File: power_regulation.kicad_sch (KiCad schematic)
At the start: 101 parts, among them IC2 PJA3402_R1_00001, IC3 MIE1W0505BGLVH-3R-P, J12 Conn_01x02_Pin, J6 V_bat_secondary, J7 Conn_01x02_Pin, J8 Conn_01x02_Pin, J9 Conn_01x02_Pin, U10 TPS7A2045PDBVR, U11 TPS7A2018PDBVRG4, U12 TPS7A2033PDBVR, U13 TPS7A2033PDBVR, U14 TLV75733PDYDR, U15 TPS7A2033PDBVR, U5 TPS7A2042PDBVRG4, U6 MCP1501-30xCH, U7 TPS62933, U8 TPS62933, U9 OPA387DBVR

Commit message: Commit before 5V rebase.
[KiCad Version: 10.0.4]
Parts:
- added C? (x4): 1u, Capacitor_SMD:C_0603_1608Metric_Pad1.08x0.95mm_HandSolder, symbol Device:C
- added R32: 100k, Resistor_SMD:R_0603_1608Metric_Pad0.98x0.95mm_HandSolder, symbol Device:R
- added U?: TPS7A2033PDBVR, Package_TO_SOT_SMD:SOT-23-5, symbol Regulator_Linear:TPS7A0508PDBV
- added Vref?: TestPoint, TestPoint:TestPoint_Pad_D1.0mm, symbol Connector:TestPoint
- C74: renamed from C64; now not fitted; now left out of the parts list
- renumbered C34 to C41, C35 to C42, C36 to C43, C37 to C44, C38 to C45, C39 to C46, C40 to C47, C41 to C48, C42 to C49, C43 to C50, C44 to C51, C45 to C52, C46 to C53, C47 to C54, C48 to C55, C49 to C56, C50 to C57, C51 to C58, C52 to C59, C53 to C60, C54 to C61, C55 to C62, C105 to C63, C56 to C64, C57 to C65, C58 to C66, C59 to C67, C60 to C68, C61 to C69, C62 to C70, C63 to C71, C67 to C72, C70 to C73, C65 to C75, C66 to C76, C68 to C77, C75 to C78, C69 to C79, C71 to C80, C72 to C81, C73 to C82, C80 to C83, C100 to C84, C74 to C85, C101 to C86, C76 to C87, C98 to C88, C77 to C89, C78 to C90, C79 to C91, C99 to C92, C81 to C93, C102 to C94, C82 to C95, C103 to C96, C104 to C97, D3 to D5, D4 to D6, J7 to J10, J8 to J11, J9 to J12, J12 to J13, J6 to J9, R21 to R20, R22 to R21, R23 to R22, R24 to R23, R25 to R24, R26 to R25, R27 to R26, R28 to R27, R29 to R28, R30 to R29, R31 to R30, R32 to R31, U9 to U10, U10 to U11, U11 to U13, U13 to U14, U14 to U15, U15 to U16, U5 to U6, U6 to U7, U7 to U8, U8 to U9
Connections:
- net +3V3_Ana: now also C?.2, C?.2, U?.5 (OUT), Vref?.1
- net +4V2_bus: no longer C44.2, C45.2, C46.2, U6.5 (OUT), U7.4 (~{SHDN}), U7.6 (VDD)
- net +5V_buck_out: no longer C59.2, C62.2, C70.2, C71.2, C82.2, IC3.10 (VIN_2), IC3.14 (VIN_3), IC3.8 (EN), IC3.9 (VIN_1), Lw1.2, R25.1, U11.1 (IN), U11.3 (EN), U15.1 (IN), U15.3 (EN)
- net GND: now also C?.1, C?.1, C?.1, C?.1, U?.2 (GND)
- new net: C44.2, C45.2, C46.2, U6.5 (OUT), U7.4 (~{SHDN}), U7.6 (VDD)
- new net: IC3.8 (EN), R32.2
- new net +5V_Ana_Bus: C?.2, C?.2, U?.1 (IN), U?.3 (EN)
- new net +Buck_Out: C59.2, C62.2, C70.2, C71.2, C82.2, IC3.10 (VIN_2), IC3.14 (VIN_3), IC3.9 (VIN_1), Lw1.2, R25.1, R32.1, U11.1 (IN), U11.3 (EN), U15.1 (IN), U15.3 (EN)
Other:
- note added: "3,3V ANALOG SUPPLY LDO Supplies Load Cell, Load Cell ADC and the 1V8 LDO"
- note added: "Isolating DCDC Converter for Voltage Measurement"
- note added: "SAR ADC Vref Driver"
- note added: "TODO: Change symbol to MCP1502!!!"
- note added: "TODO: Check Min / Max stable capacitances for the LDOS"
- note removed: "TARKASTA MINIMI STABLE KAPASITANSSIT TÄLLE !!"
- note removed: "TÄHÄN MCP1502 !!!"
- moved on the sheet: C70, C71, C75, C77, C79, C81, C82, C85, C89, C90, C93, C95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

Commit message: Implemented SAR ADC Buffering on top layer with one OPA387
[KiCad Version: 10.0.4]
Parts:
- removed C41, C42, C44, C45, C66, C? (x4): 1u, Capacitor_SMD:C_0603_1608Metric_Pad1.08x0.95mm_HandSolder, symbol Device:C
- removed C83, C85, C90, C93: 2.2u, Capacitor_SMD:C_0603_1608Metric_Pad1.08x0.95mm_HandSolder, symbol Device:C
- removed C94: 22u, Capacitor_SMD:C_1206_3216Metric_Pad1.33x1.80mm_HandSolder, symbol Device:C
- removed IC2: PJA3402_R1_00001, SOT95P240X110-3N, symbol SamacSys_Parts:PJA3402_R1_00001
- removed J10: Conn_01x02_Pin, Connector_PinHeader_2.54mm:PinHeader_1x02_P2.54mm_Vertical, symbol Connector:Conn_01x02_Pin
- removed R30: 220, Resistor_SMD:R_0603_1608Metric_Pad0.98x0.95mm_HandSolder, symbol Device:R
- removed U6: TPS7A2042PDBVRG4, Package_TO_SOT_SMD:SOT-23-5, symbol Regulator_Linear:TPS7A0508PDBV
- removed U?: TPS7A2033PDBVR, Package_TO_SOT_SMD:SOT-23-5, symbol Regulator_Linear:TPS7A0508PDBV
- removed Vref?: TestPoint, TestPoint:TestPoint_Pad_D1.0mm, symbol Connector:TestPoint
- added C101, C102, C104, C49, C61, C64, C65, C70, C75, C79, C80, C81, C82, C88: 1u, Capacitor_SMD:C_0603_1608Metric_Pad1.08x0.95mm_HandSolder, symbol Device:C
- added C62: 4.7nF, Capacitor_SMD:C_0603_1608Metric_Pad1.08x0.95mm_HandSolder, symbol Device:C
- added C72: 10u, Capacitor_SMD:C_0603_1608Metric_Pad1.08x0.95mm_HandSolder, symbol Device:C
- added DIO2: TestPoint, TestPoint:TestPoint_Pad_D1.0mm, symbol Connector:TestPoint
- added IC?: OPA2387DR, SOIC127P600X175-8N, symbol SamacSys_Parts:OPA2387DR
- added R32: 0R, Resistor_SMD:R_0603_1608Metric_Pad0.98x0.95mm_HandSolder, symbol Device:R
- added U12, U15: TPS7A2050PDBVR, Package_TO_SOT_SMD:SOT-23-5, symbol Regulator_Linear:TPS7A0508PDBV
- added U14: TPS7A2033PDBVR, Package_TO_SOT_SMD:SOT-23-5, symbol Regulator_Linear:TPS7A0508PDBV
- C60: now fitted
- C68: renamed from C67; value 10u -> 1u
- C78, C87, C89, C91: value 2.2u -> 1u
- C84, C86: value 22u -> 1u; footprint Capacitor_SMD:C_1206_3216Metric_Pad1.33x1.80mm_HandSolder -> Capacitor_SMD:C_0603_1608Metric_Pad1.08x0.95mm_HandSolder; now fitted; now in the parts list
- R25: value 52.3k -> 63k
- R29: renamed from R22; value 7.87k -> 8.2k
- R30: renamed from R24; value 11k -> 10k
- R33: renamed from R29; value 5R -> 1R
- R35: renamed from R33; now not fitted; now left out of the parts list
- R36: renamed from R34; now not fitted; now left out of the parts list
- R37: renamed from R35; now not fitted; now left out of the parts list
- U10: renamed from U11; value TPS7A2045PDBVR -> TPS7A2055PDBVR; Manufacturing_Number TPS7A2045PDBVR -> TPS7A2055PDBVR; Mouser_nro (none) -> 595-TPS7A2055PDBVR
- U17: renamed from U12; value TPS7A2033PDBVR -> TPS7A2050PDBVR; Manufacturing_Number (none) -> TPS7A2050PDBVR
- U18: renamed from U16; value TPS7A2033PDBVR -> TPS7A2045PDBVR; Manufacturing_Number (none) -> TPS7A2045PDBVR
- U8: renamed from U7; value MCP1501-30xCH -> MCP1502T-50E/CHY
- renumbered C96 to C100, C97 to C103, C95 to C105, C50 to C43, C47 to C44, C52 to C45, C48 to C46, C49 to C47, C54 to C48, C46 to C50, C43 to C51, C55 to C52, C57 to C53, C51 to C54, C61 to C55, C53 to C56, C59 to C57, C62 to C58, C56 to C59, C58 to C63, C82 to C66, C63 to C67, C64 to C69, C65 to C71, C68 to C73, C69 to C74, C80 to C77, C70 to C83, C71 to C85, C74 to C90, C88 to C92, C92 to C93, C75 to C94, C72 to C95, C79 to C96, C77 to C97, C73 to C98, C81 to C99, J11 to J10, J12 to J11, J13 to J12, R21 to R22, R20 to R24, R32 to R34, U15 to U11, U14 to U13, U13 to U16, U8 to U6, U9 to U7, U10 to U9
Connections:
- net +4V2_bus is gone; now on net +5V5_bus: C63.2, U9.5 (V+)
- net +5V_buck_out is gone; now on net GND: C60.1
- net +1V8_MCP_AVIN: now also C101.2, C104.2; no longer C89.2
- net +3V3_DIO: now also C84.2, C86.2; no longer C87.2, C91.2
- net +3V3_ESP: now also C72.2
- net GND: now also C101.1, C102.1, C104.1, C49.1, C61.2, C64.1, C65.2, C70.2, C72.1, C75.1, C79.1, C80.1, C81.1, C82.1, C88.1, U12.2 (GND), U14.2 (GND), U15.2 (GND); no longer C60.2, R31.1
- net +5V5_bus: now reaches C50.2, U8.4 (~{SHDN}), U8.6 (VDD)
- net +5V5_bus: now also C68.1, C73.2, C74.2, C76.2, C77.2, C95.2, C98.2, U10.5 (OUT), U13.1 (IN), U13.3 (EN), U17.1 (IN), U17.3 (EN), C49.2, C70.1, C80.2, C82.2, U15.1 (IN), U15.3 (EN)
- net +12V_Fan_Supply: now reaches D6.2 (A), J10.2 (Pin_2)
- net +5V_Vref: now reaches R31.2
- net +5V_Vref: now also C67.2, C69.2, C71.2, R33.2, Vref1.1
- net at C59.2, R33.1, U9.1: now also R32.2
- net at R30.2, U9.3 (+): now also C60.2
- net +3V3_Ana renamed +5V_Ana
- net +5V_Ana: now also C89.2, C91.2, Vref2.1, C79.2, U14.1 (IN), U14.3 (EN), U15.5 (OUT); no longer C84.2, C86.2, U17.5 (OUT), Vref3.1
- net +3V3_ISO renamed +4V5_ISO
- removed net +3V_Vref: C67.2, C69.2, C71.2, R33.2, U9.4 (-), Vref1.1
- removed net +4V5_bus: C68.1, C73.2, C74.2, C76.2, C77.2, C95.2, C98.2, U10.5 (OUT), U13.1 (IN), U13.3 (EN), U17.1 (IN), U17.3 (EN), Vref2.1
- net +Buck_Out renamed +6V_Buck_Out
- net +6V_Buck_Out: now also C61.1, C64.2, C65.1, C75.2, U12.1 (IN), U12.3 (EN); no longer C83.2, C85.2, IC3.10 (VIN_2), IC3.14 (VIN_3), IC3.9 (VIN_1), R34.1
- new net: C62.1, R32.1
- new net: C62.2, R31.1, U9.4 (-)
- new net: C81.2, C83.2, C85.2, IC3.10 (VIN_2), IC3.14 (VIN_3), IC3.9 (VIN_1), R34.1, U12.5 (OUT)
- new net +3V3_LC: C87.2, C88.2, DIO2.1, U14.5 (OUT)
- new net +5V_Cur_Sensor: C102.2, U17.5 (OUT), Vref3.1
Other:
- note added: "(Can be used to improve perfomance)"
- note added: "12V Fan Supply"
- note added: "3V3 Digital Supply"
- note added: "3V3 Load Cell Supply"
- note added: "5,0V Analog Bus"
- note added: "5,0V Current Sensor Sypply"
- note added: "5V5 Instrument Supply Bus"
- note added: "ESP32 3,3V SUPPLY LDO"
- note added: "Hall-based current sensors have noisy inputs, so it was separated from the other Analog supplies"
- note added: "MCP33131 AVIN 1,8V REF Supply"
- note added: "Max Input supply voltage: 6.0 V Max C_out: 200 uF Max I_out: 300 mA"
- note added: "Maximum Temperature Coefficient: 7 ppm/°C from -40°C to +125°C Initial Accuracy: 0.1% Min Supply Vdd+0.2V Variants ... 4.096V,4.5V,5V"
- note added: "Single supply: 1.7 V to 5.5 V Swing: 5 mV from rails 1/f noise: 177 nVPP (0.1 Hz to 10 Hz) Ultra-low offset voltage: ±2 µV Zero drift: ±0.003 µV/°C Low-input bias current: 150 pA Low noise: 8.5 nV√Hz at 1 kHz Gain bandwidth: 5.7 MHz High linearity output swing range: (V-) + 0.150 (V+) - 0.150"
- note added: "TODO: FIND PROPER 6V 800mA INPUT TO 3V3 LDO"
- note added: "~6V Measurement Circuitry Primary Supply Bus"
- note removed: "12V Bus"
- note removed: "3,3V ANALOG SUPPLY LDO"
- note removed: "3,3V ANALOG SUPPLY LDO Supplies Load Cell, Load Cell ADC and the 1V8 LDO"
- note removed: "3,3V DIGITAL SUPPLY LDO"
- note removed: "5V Bus to Low Noise 4.2V LDO"
- note removed: "Buck Stage outputs 5.0V This is fed to the LDO that is feeding the 4.5V Bus"
- note removed: "ESP32 3,3V SUPPLY LDO 800mA"
- note removed: "MCP33131 AVIN 1,8V REF"
- note removed: "SAR ADC 3,0V REF"
- note removed: "TODO: Change symbol to MCP1502!!!"
- note removed: "VARMISTA ETTÄ PINNIT JA FOOTPRINT OIKEAT: PJA3402_R1_00001 SOT-23-3"
- moved on the sheet: C100, C103, C105, C43, C44, C45, C46, C47, C48, C50, C51, C52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

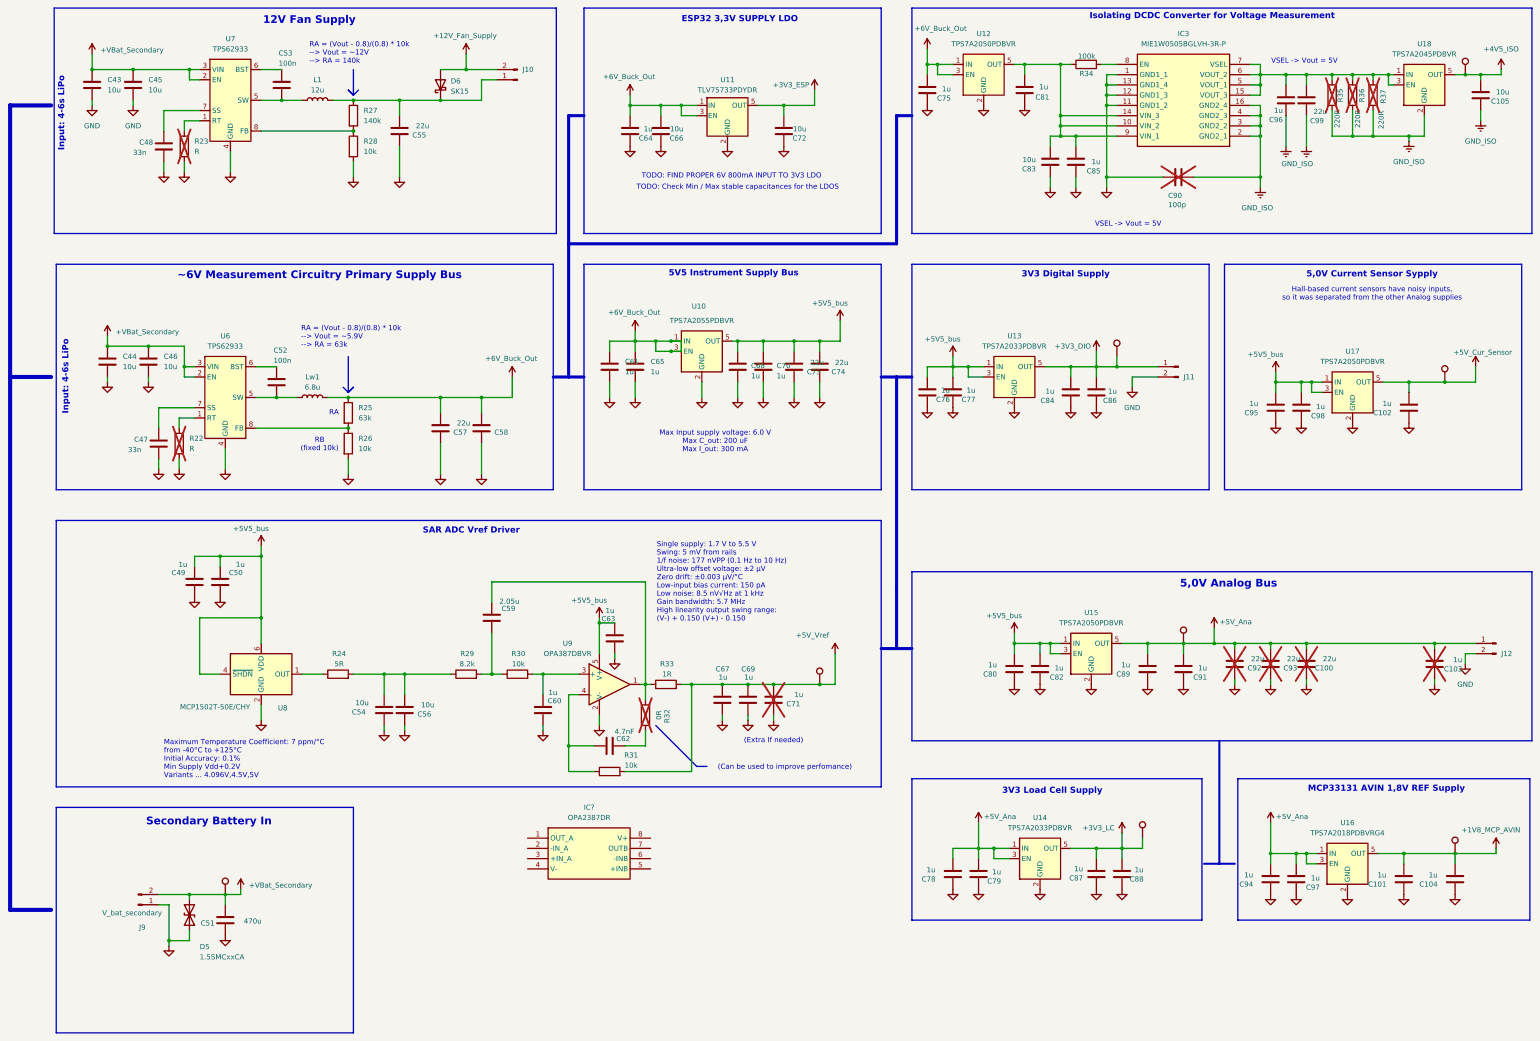
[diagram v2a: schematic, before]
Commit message: Implemented dual SAR ADC Buffering and Current sensor ratiometric supply
[KiCad Version: 10.0.4]
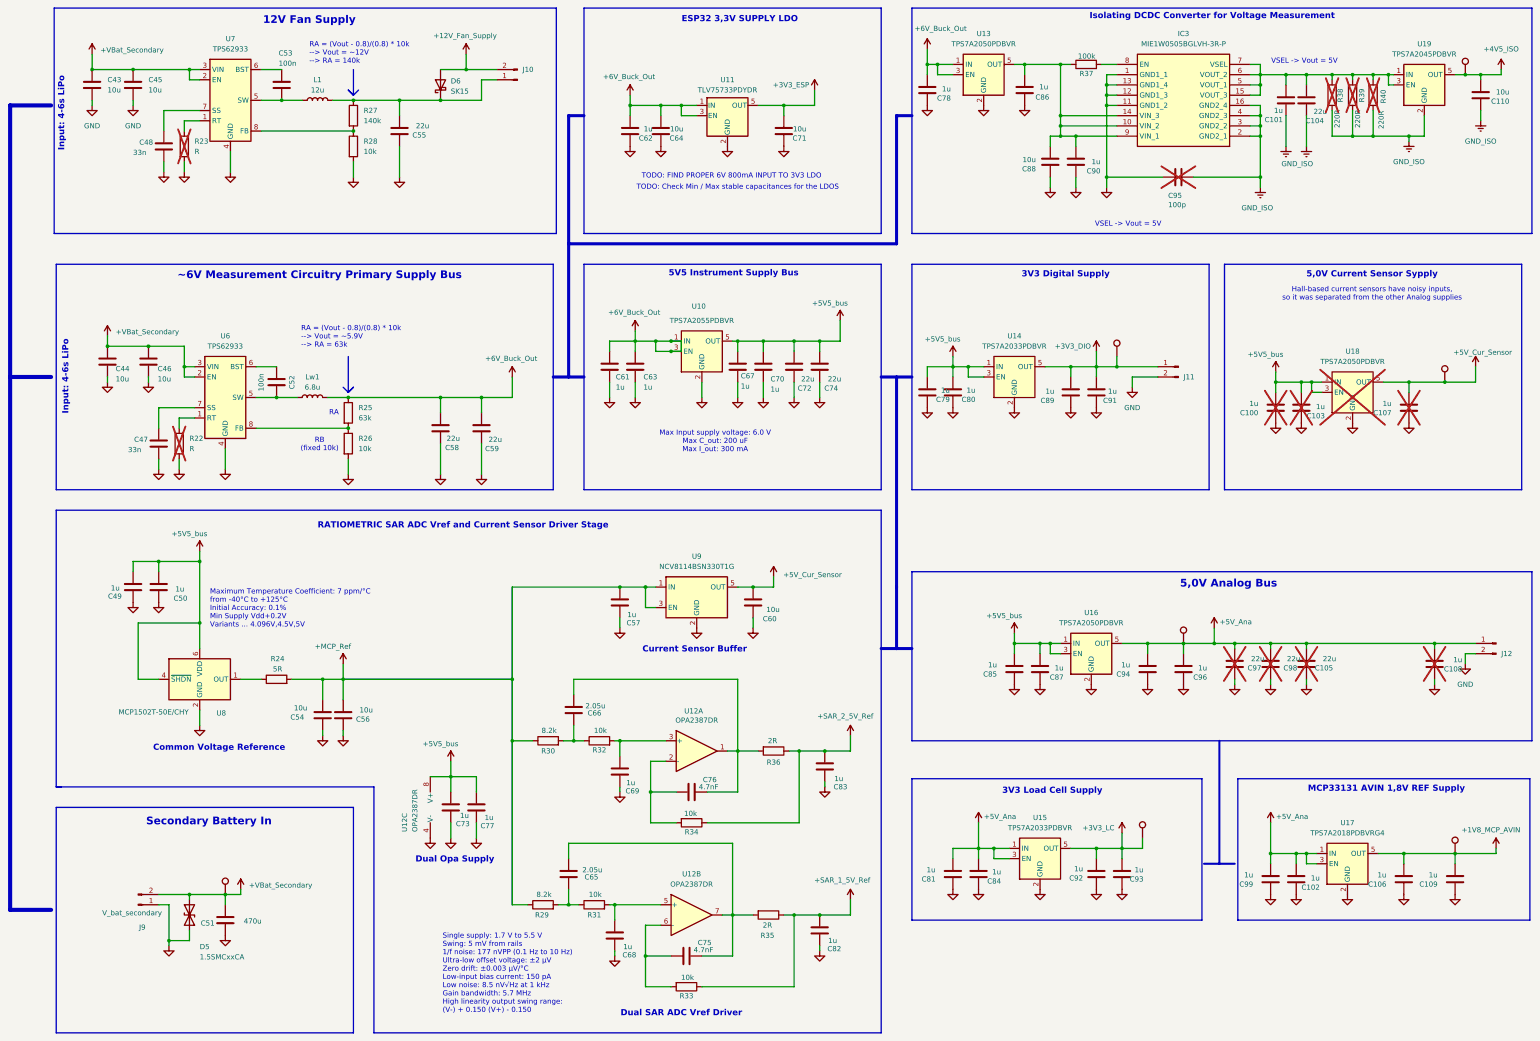
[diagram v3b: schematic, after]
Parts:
- removed C59: 2.05u, Capacitor_SMD:C_0603_1608Metric_Pad1.08x0.95mm_HandSolder, symbol Device:C
- removed C62: 4.7nF, Capacitor_SMD:C_0603_1608Metric_Pad1.08x0.95mm_HandSolder, symbol Device:C
- removed C63, C67, C71: 1u, Capacitor_SMD:C_0603_1608Metric_Pad1.08x0.95mm_HandSolder, symbol Device:C
- removed IC?: OPA2387DR, SOIC127P600X175-8N, symbol SamacSys_Parts:OPA2387DR
- removed U9: OPA387DBVR, Package_TO_SOT_SMD:SOT-23-5, symbol Amplifier_Operational:OPA376xxDBV
- removed Vref1: TestPoint, TestPoint:TestPoint_Pad_D1.0mm, symbol Connector:TestPoint
- added C57, C68, C73, C77, C82, C83: 1u, Capacitor_SMD:C_0603_1608Metric_Pad1.08x0.95mm_HandSolder, symbol Device:C
- added C65, C66: 2.05u, Capacitor_SMD:C_0603_1608Metric_Pad1.08x0.95mm_HandSolder, symbol Device:C
- added C75, C76: 4.7nF, Capacitor_SMD:C_0603_1608Metric_Pad1.08x0.95mm_HandSolder, symbol Device:C
- added R34: 10k, Resistor_SMD:R_0603_1608Metric_Pad0.98x0.95mm_HandSolder, symbol Device:R
- added R35, R36: 2R, Resistor_SMD:R_0603_1608Metric_Pad0.98x0.95mm_HandSolder, symbol Device:R
- added U12: OPA2387DR, Package_SO:SOIC-8_3.9x4.9mm_P1.27mm, symbol Amplifier_Operational:OPA2325
- added U9: NCV8114BSN330T1G, Package_SO:SOIC-8_3.9x4.9mm_P1.27mm, symbol Regulator_Linear:NCV8114BSN330T1G
- C100: renamed from C95; now not fitted
- C103: renamed from C98; now not fitted
- C107: renamed from C102; now not fitted
- C60: value 1u -> 10u
- R30: value 10k -> 8.2k
- R32: value 0R -> 10k; now fitted; now in the parts list
- R33: value 1R -> 10k
- U18: renamed from U17; now not fitted
- renumbered C96 to C101, C97 to C102, C99 to C104, C100 to C105, C101 to C106, C103 to C108, C104 to C109, C105 to C110, C57 to C58, C58 to C59, C64 to C62, C65 to C63, C66 to C64, C68 to C67, C72 to C71, C73 to C72, C75 to C78, C76 to C79, C77 to C80, C78 to C81, C79 to C84, C80 to C85, C81 to C86, C82 to C87, C83 to C88, C84 to C89, C85 to C90, C86 to C91, C87 to C92, C88 to C93, C89 to C94, C90 to C95, C91 to C96, C92 to C97, C93 to C98, C94 to C99, R34 to R37, R35 to R38, R36 to R39, R37 to R40, U12 to U13, U13 to U14, U14 to U15, U15 to U16, U16 to U17, U18 to U19, Vref2 to Vref1, Vref3 to Vref2, Vref4 to Vref3
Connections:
- net +5V5_bus: now also C73.2, C77.2, U12.8 (V+)
- net +5V_Cur_Sensor: now also C60.2, U9.5 (OUT)
- net GND: now also C57.1, C68.1, C73.1, C77.1, C82.1, C83.1, U12.4 (V-), U9.2 (GND)
- net at R32.1: now also R30.2, C66.1
- net at R31.1: now also R29.2, C65.1
- net +MCP_Ref: now reaches C54.2, C56.2, R24.2, R29.1
- net +MCP_Ref: now also R30.1, C57.2, U9.1 (IN), U9.3 (EN)
- net at R32.2: now also C69.2, U12.3 (+); no longer R33.1
- removed net +5V_Vref: C69.2, R31.2, R33.2
- new net: C75.1, R33.2, U12.6 (-)
- new net: C65.2, C75.2, R35.2, U12.7
- new net: C76.1, R34.2, U12.2 (-)
- new net: C66.2, C76.2, R36.2, U12.1
- new net: C68.2, R31.2, U12.5 (+)
- new net +SAR_1_5V_Ref: C82.2, R33.1, R35.1
- new net +SAR_2_5V_Ref: C83.2, R34.1, R36.1
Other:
- note added: "Common Voltage Reference"
- note added: "Current Sensor Buffer"
- note added: "Dual Opa Supply"
- note added: "Dual SAR ADC Vref Driver"
- note added: "RATIOMETRIC SAR ADC Vref and Current Sensor Driver Stage"
- note removed: "(Can be used to improve perfomance)"
- note removed: "(Extra If needed)"
- note removed: "SAR ADC Vref Driver"
- moved on the sheet: C49, C50, C54, C56, R24, U8
